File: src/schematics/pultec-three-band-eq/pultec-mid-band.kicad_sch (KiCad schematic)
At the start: 30 parts, among them J14 Mid bst/cut switch, J15 Mid Sel Ret, J16 Mid Sel Ret, J17 2H, J18 1H, J26 .45H, J27 .22H, J28 .1H, J29 Mid Lvl (47 Log), J30 Mid Sel Snd

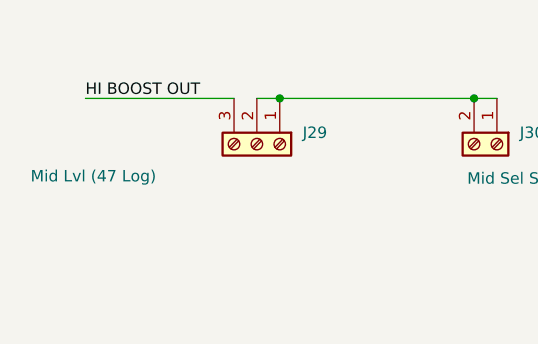
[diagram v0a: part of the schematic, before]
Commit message: - fixed issue with hierarchical label - fixed unrouted trace related to issue with hierarchical label - Updated PCB identifier in front copper and front fab layers to use variables instead of hard-coded dates and revisions.
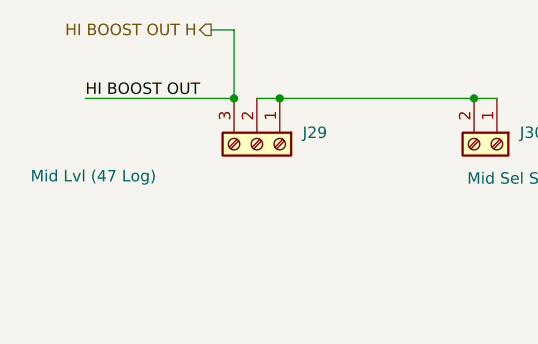
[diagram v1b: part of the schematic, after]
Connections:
- net HI BOOST OUT renamed HI BOOST OUT H
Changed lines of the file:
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@@
+	)
+	(junction
+		(at 69.85 50.8)
+		(diameter 0)
+		(color 0 0 0 0)
 	)
 	(junction
@@
 	(wire
 		(pts
+			(xy 67.31 43.18) (xy 69.85 43.18)
+		)
+		(stroke
+			(width 0)
+			(type default)
+		)
+	)
+	(wire
+		(pts
 			(xy 48.26 173.99) (xy 48.26 180.34)
 		)
@@
 		(pts
 			(xy 184.15 93.98) (xy 184.15 110.49)
+		)
+		(stroke
+			(width 0)
+			(type default)
+		)
+	)
+	(wire
+		(pts
+			(xy 69.85 43.18) (xy 69.85 50.8)
 		)
 		(stroke
@@
 		)
 	)
+	(hierarchical_label "HI BOOST OUT H"
+		(shape output)
+		(at 67.31 43.18 180)
+		(fields_autoplaced yes)
+		(effects
+			(font
+				(size 1.27 1.27)
+			)
+			(justify right)
+		)
+	)

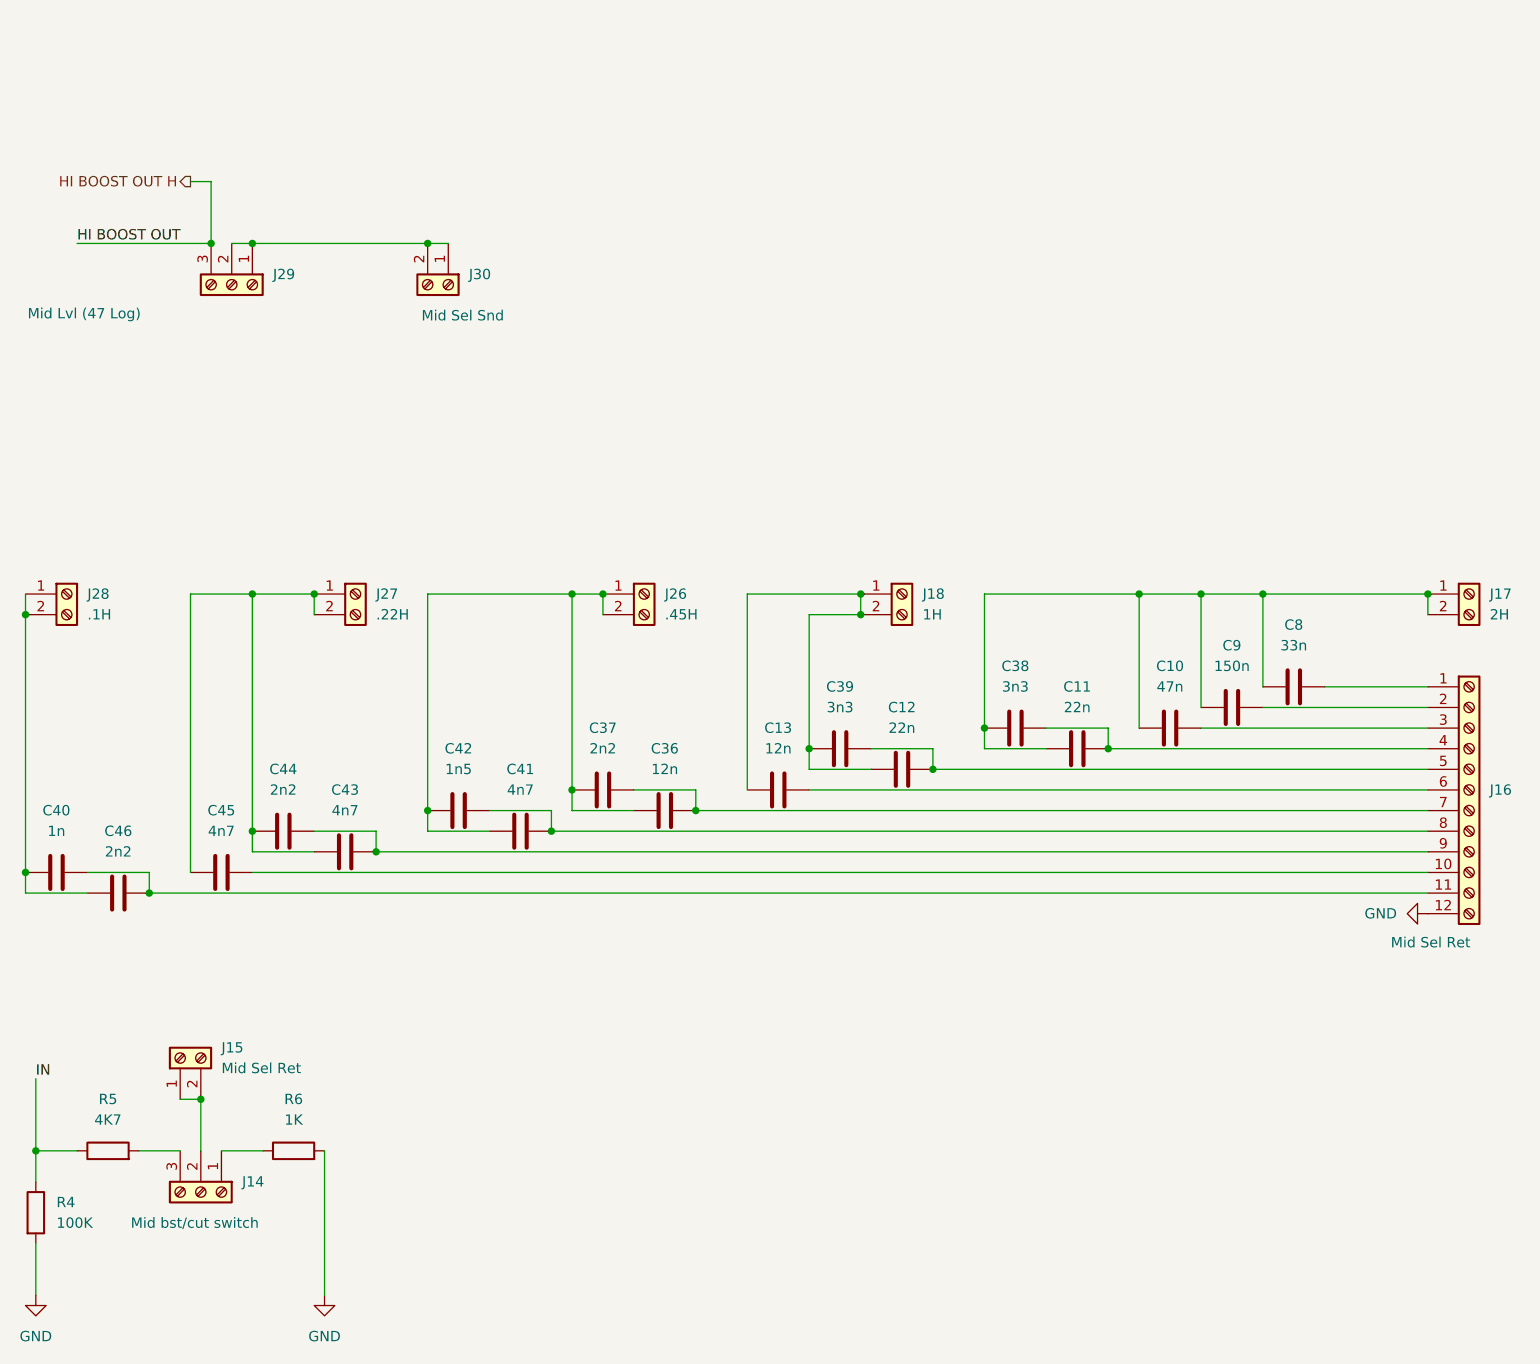
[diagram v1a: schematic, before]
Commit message: - re-worked the mid-range - exported gerbers for PCB manufacture
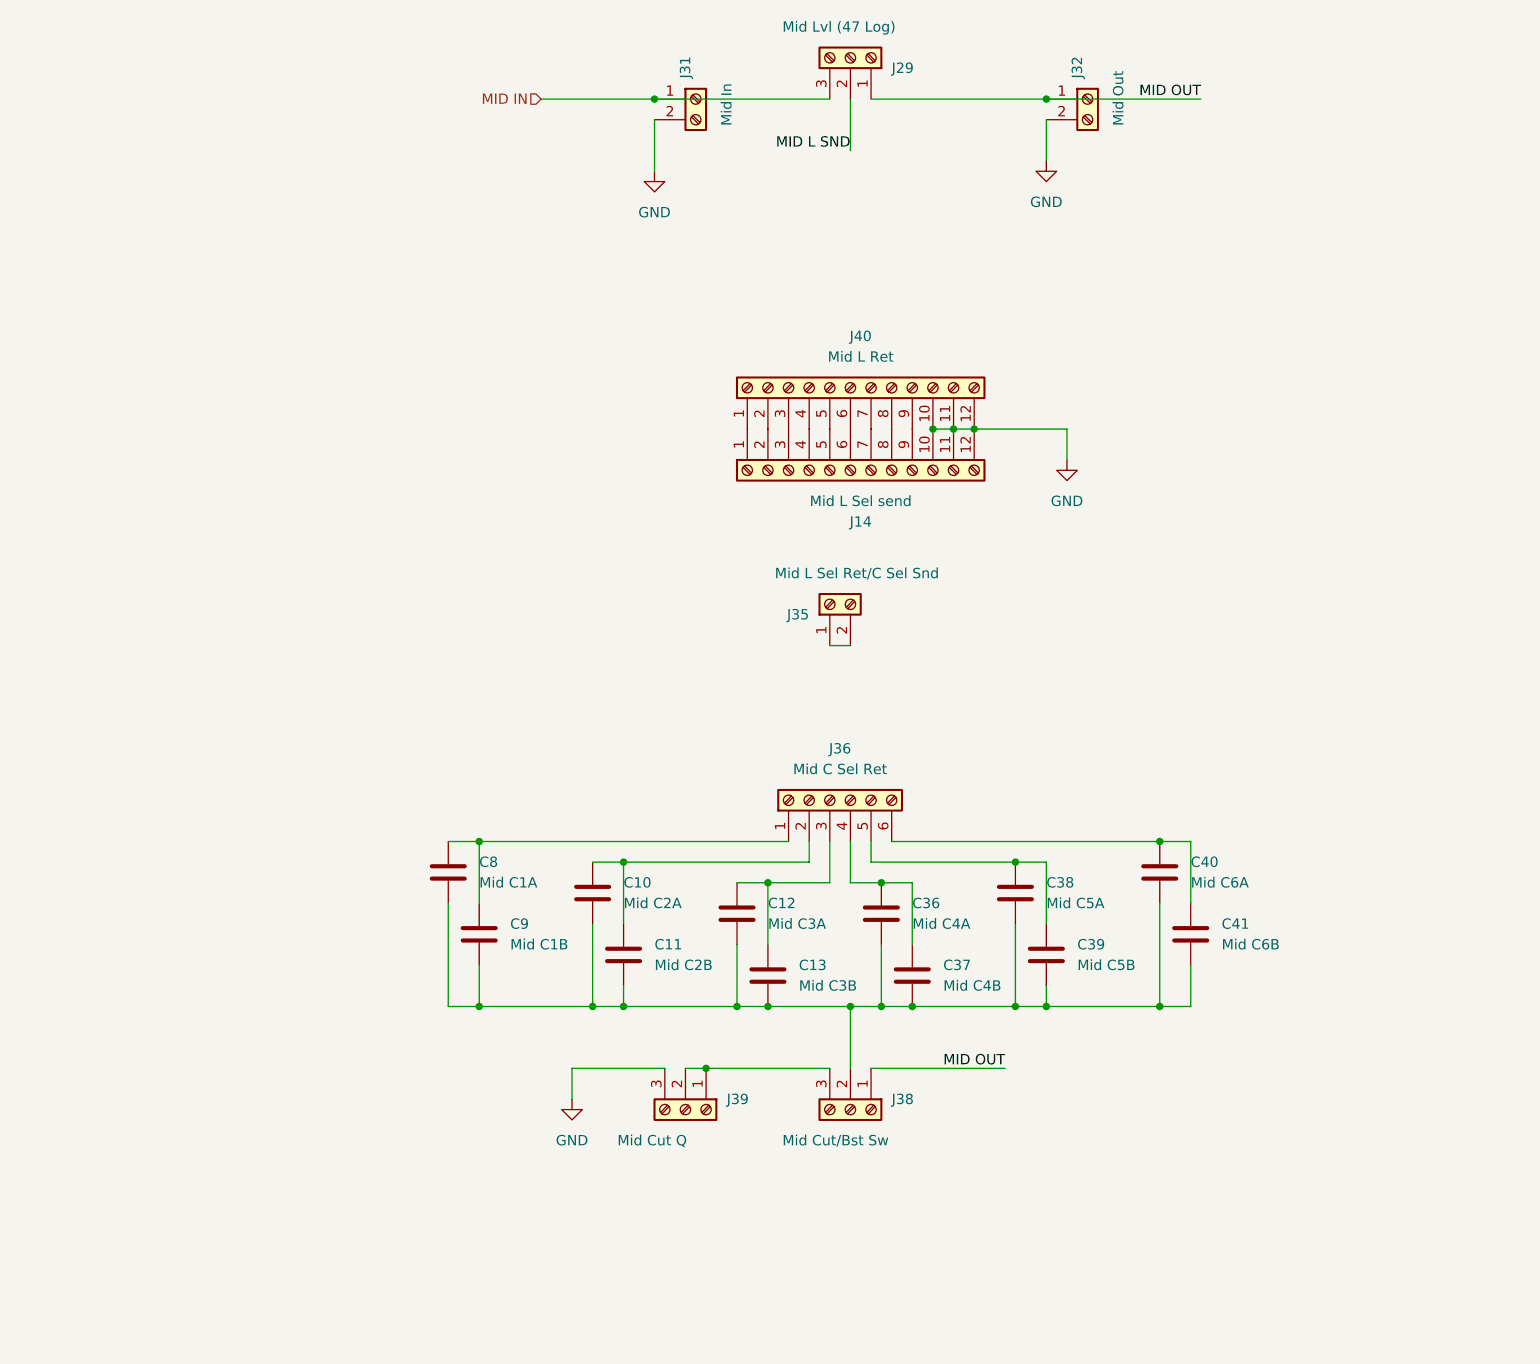
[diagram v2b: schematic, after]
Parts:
- removed C42: 1n5, OL Library:C_Rect_L7.0mm_W2.0mm_P5.00mm_Fat_Pad, symbol Device:C
- removed C43, C45: 4n7, OL Library:C_Rect_L7.0mm_W2.0mm_P5.00mm_Fat_Pad, symbol Device:C
- removed C44, C46: 2n2, OL Library:C_Rect_L7.0mm_W2.0mm_P5.00mm_Fat_Pad, symbol Device:C
- removed J14: Mid bst/cut switch, OL Library:TerminalBlock_Phoenix_MKDS-1,5-3_1x03_P5.00mm_Horizontal Fat Pad, symbol Connector:Screw_Terminal_01x03
- removed J15: Mid Sel Ret, OL Library:TerminalBlock_Phoenix_MKDS-1,5-2_1x02_P5.00mm_Horizontal Fat Pad, symbol Connector:Screw_Terminal_01x02
- removed J16: Mid Sel Ret, OL Library:TerminalBlock_Phoenix_MKDS-1,5-12_1x12_P5.00mm_Horizontal_Fat_Pad, symbol Connector:Screw_Terminal_01x12
- removed J17: 2H, OL Library:TerminalBlock_Phoenix_MKDS-1,5-2_1x02_P5.00mm_Horizontal Fat Pad, symbol Connector:Screw_Terminal_01x02
- removed J18: 1H, OL Library:TerminalBlock_Phoenix_MKDS-1,5-2_1x02_P5.00mm_Horizontal Fat Pad, symbol Connector:Screw_Terminal_01x02
- removed J26: .45H, OL Library:TerminalBlock_Phoenix_MKDS-1,5-2_1x02_P5.00mm_Horizontal Fat Pad, symbol Connector:Screw_Terminal_01x02
- removed J27: .22H, OL Library:TerminalBlock_Phoenix_MKDS-1,5-2_1x02_P5.00mm_Horizontal Fat Pad, symbol Connector:Screw_Terminal_01x02
- removed J28: .1H, OL Library:TerminalBlock_Phoenix_MKDS-1,5-2_1x02_P5.00mm_Horizontal Fat Pad, symbol Connector:Screw_Terminal_01x02
- removed J30: Mid Sel Snd, OL Library:TerminalBlock_Phoenix_MKDS-1,5-2_1x02_P5.00mm_Horizontal Fat Pad, symbol Connector:Screw_Terminal_01x02
- removed R4: 100K, OL Library:R_Axial_DIN0207_L6.3mm_D2.5mm_P7.62mm_Horizontal, symbol Device:R
- removed R5: 4K7, OL Library:R_Axial_DIN0207_L6.3mm_D2.5mm_P7.62mm_Horizontal, symbol Device:R
- removed R6: 1K, OL Library:R_Axial_DIN0207_L6.3mm_D2.5mm_P7.62mm_Horizontal, symbol Device:R
- added J14: Mid L Sel send, OL Library:TerminalBlock_Phoenix_MKDS-1,5-12_1x12_P5.00mm_Horizontal_Fat_Pad, symbol Connector:Screw_Terminal_01x12
- added J31: Mid In, OL Library:TerminalBlock_Phoenix_MKDS-1,5-2_1x02_P5.00mm_Horizontal Fat Pad, symbol Connector:Screw_Terminal_01x02
- added J32: Mid Out, OL Library:TerminalBlock_Phoenix_MKDS-1,5-2_1x02_P5.00mm_Horizontal Fat Pad, symbol Connector:Screw_Terminal_01x02
- added J35: Mid L Sel Ret/C Sel Snd, OL Library:TerminalBlock_Phoenix_MKDS-1,5-2_1x02_P5.00mm_Horizontal Fat Pad, symbol Connector:Screw_Terminal_01x02
- added J36: Mid C Sel Ret, OL Library:TerminalBlock_Phoenix_MKDS-1,5-6_1x06_P5.00mm_Horizontal_Fat_Pad, symbol Connector:Screw_Terminal_01x06
- added J38: Mid Cut/Bst Sw, OL Library:TerminalBlock_Phoenix_MKDS-1,5-3_1x03_P5.00mm_Horizontal Fat Pad, symbol Connector:Screw_Terminal_01x03
- added J39: Mid Cut Q, OL Library:TerminalBlock_Phoenix_MKDS-1,5-3_1x03_P5.00mm_Horizontal Fat Pad, symbol Connector:Screw_Terminal_01x03
- added J40: Mid L Ret, OL Library:TerminalBlock_Phoenix_MKDS-1,5-12_1x12_P5.00mm_Horizontal_Fat_Pad, symbol Connector:Screw_Terminal_01x12
- C10: value 47n -> Mid C2A
- C11: value 22n -> Mid C2B
- C12: value 22n -> Mid C3A
- C13: value 12n -> Mid C3B
- C36: value 12n -> Mid C4A
- C37: value 2n2 -> Mid C4B
- C38: value 3n3 -> Mid C5A
- C39: value 3n3 -> Mid C5B
- C40: value 1n -> Mid C6A
- C41: value 4n7 -> Mid C6B
- C8: value 33n -> Mid C1A
- C9: value 150n -> Mid C1B
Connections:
- net GND: now also J14.10 (Pin_10), J14.11 (Pin_11), J14.12 (Pin_12), J31.2 (Pin_2), J32.2 (Pin_2), J39.3 (Pin_3), J40.10 (Pin_10), J40.11 (Pin_11), J40.12 (Pin_12)
- net at C40.1: now also C41.1, J36.6 (Pin_6)
- net at C40.2: now also C10.2, C11.2, C12.2, C13.2, C36.2, C37.2, C38.2, C39.2, C41.2, C8.2, C9.2, J38.2 (Pin_2)
- net at C12.1, C13.1: now also J36.3 (Pin_3); no longer C39.1
- net at C36.1, C37.1: now also J36.4 (Pin_4); no longer C41.1
- net MID L SND: now reaches J29.2 (Pin_2)
- net MID L SND: no longer J29.1 (Pin_1)
- net HI BOOST OUT H renamed MID IN
- net MID IN: now also J31.1 (Pin_1)
- new net: C38.1, C39.1, J36.5 (Pin_5)
- new net: C8.1, C9.1, J36.1 (Pin_1)
- new net: J38.3 (Pin_3), J39.1 (Pin_1), J39.2 (Pin_2)
- new net: C10.1, C11.1, J36.2 (Pin_2)
- new net: J14.1 (Pin_1), J40.1 (Pin_1)
- new net: J14.2 (Pin_2), J40.2 (Pin_2)
- new net: J14.3 (Pin_3), J40.3 (Pin_3)
- new net: J14.4 (Pin_4), J40.4 (Pin_4)
- new net: J14.5 (Pin_5), J40.5 (Pin_5)
- new net: J14.6 (Pin_6), J40.6 (Pin_6)
- new net: J14.7 (Pin_7), J40.7 (Pin_7)
- new net: J14.8 (Pin_8), J40.8 (Pin_8)
- new net: J14.9 (Pin_9), J40.9 (Pin_9)
- new net: J35.1 (Pin_1), J35.2 (Pin_2)
- new net MID OUT: J29.1 (Pin_1), J32.1 (Pin_1), J38.1 (Pin_1)
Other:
- moved on the sheet: J29
